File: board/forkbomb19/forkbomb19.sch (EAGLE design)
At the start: 30 parts, among them U1 ESP-WROOM-03

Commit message: drew the tv and started placing stuff
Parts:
- removed U$1: TLC59116-Q1, forkbomb19:TLC59116-Q1
- added C10, C13, C14: 10uF, resistor:C-USC1210
- added C11: 2.2uF, adafruit:C-USC0805
- added C12: 0.1uF, adafruit:C-USC0805
- added C62: 1F, resistor:CPOL-USE5-8.5
- added CHRG/LBO: ORANGE, piboy_new:ADAFRUIT_LEDCHIPLED_0603
- added CN1: LIPO, adafruit:JST_2PIN-SMT-RA
- added D1: MBRS130LT3, diode:MBRS130LT3
- added DONE: GREEN, piboy_new:ADAFRUIT_LEDCHIPLED_0603
- added L1: 6.8uH, microbuilder:INDUCTORTDK_VLC5045
- added LBO: RED, piboy_new:ADAFRUIT_LEDCHIPLED_0603
- added LOGO_B, LOGO_G, LOGO_R: REVERSE_PLCC_LED, forkbomb19:REVERSE_PLCC_LED
- added ON: BLUE, piboy_new:ADAFRUIT_LEDCHIPLED_0603
- added R10: 1.12M, resistor:R-US_R0603
- added R11: 200K, resistor:R-US_R0603
- added R12: 340K, adafruit:R-US_R0805
- added R13: 200K, adafruit:R-US_R0805
- added R14: 1.87M, adafruit:R-US_R0805
- added R15: 270K, resistor:R-US_R0603
- added R16, R21: 100K, resistor:R-US_R0603
- added R17, R18, R20, R9: 1K, resistor:R-US_R0603
- added R19: 1.0K, resistor:R-US_R0603
- added R22: 68, resistor:R-US_R0805
- added T3: MMUN2133LT1G, piboy_new:TRANSISTOR_MUN2113T1-PNP_DRIVER-SC59-BEC
- added THERM: 15K, resistor:R-US_R0603
- added U$17: CL-SB-12A-02T, defcon:CL-SB-12A-02T
- added U4: TPS61090RSAR, microbuilder:VREG_TPS6103X
- added U5: MCP73871, microbuilder:MCP73871
- C1: value (none) -> 100nF; device resistor:C-USC0805 -> resistor:C-USC0603
- C4, C9: device resistor:C-USC0805 -> resistor:C-USC0603
- R1, R6, R7: device resistor:R-US_R0805 -> resistor:R-US_R0603
- R8: value ILED -> 68
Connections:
- removed net RDY_2_SEND: U3G$1.RTS
- new net BOOST_ENABLE: R13.2, U$17.P$2, U4.EN
- new net LBO: T3.B, U4.LBO
- new net N$16: L1.2, U4.SW
- new net N$17: R12.2, R14.1, U4.LBI
- new net N$18: LBO.A, R20.1
- new net N$19: R10.1, R11.2, U4.FB
- new net N$20: R20.2, T3.C
- new net N$21: ON.A, R9.2
- new net N$22: R15.1, R16.1, U5.VPCC
- new net N$23: R18.1, U5.STAT2
- new net N$24: R17.1, U5.STAT1/LBO
- new net N$25: R19.2, U5.PROG1
- new net N$26: THERM.2, U5.THERM
- new net N$27: DONE.C, R18.2
- new net N$28: CHRG/LBO.C, R17.2
- new net N$29: R21.2, U5.PROG3
- new net N$30: CN1.2, D1.A
- new net N$31: LOGO_G.A, R8.2
- new net VBAT: C10.1, C12.1, L1.1, R13.1, R14.2, T3.E, U4.VBAT, U5.VOUT1, U5.VOUT2
- new net VBUS: CHRG/LBO.A, DONE.A, R15.2, U5./TE, U5.CE, U5.PROG2, U5.SEL, U5.VIN1, U5.VIN2
- new net VLIPO: C14.1, D1.C, U5.VBAT1, U5.VBAT2, U5.VBATSENS
- net +3V3: now also C11.1, C13.1, C62.+, LOGO_B.A, R10.2, R22.1, R8.1, R9.1, U4.VOUT; no longer U$1.VCC
- net EN: no longer U$1.RESET
- net GND: now also C10.2, C11.2, C12.2, C13.2, C14.2, C62.-, CN1.1, LBO.C, LOGO_B.C, LOGO_G.C, LOGO_R.C, ON.C, R11.1, R12.1, R16.2, R19.1, R21.1, THERM.1, U$17.P$3, U4.GND, U4.PGND, U4.SYNC, U5.THERMAL, U5.VSS1, U5.VSS2; no longer R8.1, U$1.A0, U$1.A1, U$1.A2, U$1.A3, U$1.GND
- net I2C_SCL: no longer U$1.SCL
- net I2C_SDA: no longer U$1.SDA
- net N$12: now also LOGO_R.A, R22.2; no longer R8.2, U$1.REXT
- net RDY_2_SND: now also U3G$1.RTS
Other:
- note added: "1.0K = 1000mA"
- note added: "10K NTC Thermistor:"
- note added: "2.0K = 500mA"
- note added: "6.8uH power w/2A current"
- note added: "Charge Rate = 1000V/PROG1"
- note added: "No Thermistor:"
- note added: "RT1 = 0, RT2 = 10K"
- note added: "RT1 = TBD, RT2 = TBD"
- note added: "See Pg 15 1st para"
- moved on the sheet: C8, C9, R6, R7, R8, T1, T2, U3G$1, U3G$2, X1

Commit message: more layout work on the board
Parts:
- removed C13, C14: 10uF, resistor:C-USC1210
- removed C62: 1F, resistor:CPOL-USE5-8.5
- removed CHRG/LBO: ORANGE, piboy_new:ADAFRUIT_LEDCHIPLED_0603
- removed CN1: LIPO, adafruit:JST_2PIN-SMT-RA
- removed DONE: GREEN, piboy_new:ADAFRUIT_LEDCHIPLED_0603
- removed LBO: RED, piboy_new:ADAFRUIT_LEDCHIPLED_0603
- removed ON: BLUE, piboy_new:ADAFRUIT_LEDCHIPLED_0603
- removed R12: 340K, adafruit:R-US_R0805
- removed R13: 200K, adafruit:R-US_R0805
- removed R14: 1.87M, adafruit:R-US_R0805
- removed R15: 270K, resistor:R-US_R0603
- removed R16, R21: 100K, resistor:R-US_R0603
- removed R17, R18, R20: 1K, resistor:R-US_R0603
- removed R19: 1.0K, resistor:R-US_R0603
- removed R2: 10K, pot:TRIM_US-B64Y
- removed T3: MMUN2133LT1G, piboy_new:TRANSISTOR_MUN2113T1-PNP_DRIVER-SC59-BEC
- removed THERM: 15K, resistor:R-US_R0603
- removed U4: TPS61090RSAR, microbuilder:VREG_TPS6103X
- removed U5: MCP73871, microbuilder:MCP73871
- added D2: MBRS130LT3, diode:MBRS130LT3
- added U$1: LM2623, forkbomb19:LM2623
- added X2: 22-23-2021, con-molex:22-23-2021
- added X3: POT_GND, con-samtec:TSW-101-07-G-S
- added X4: POT_3V3, con-samtec:TSW-101-07-G-S
- added X5: POT_SIG, con-samtec:TSW-101-07-G-S
- C10: value 10uF -> 22uF; device resistor:C-USC1210 -> resistor:CPOL-US153CLV-0405
- C11: value 2.2uF -> 4.7pF; device adafruit:C-USC0805 -> resistor:C-USC0603
- C12: value 0.1uF -> 10uF; device adafruit:C-USC0805 -> resistor:CPOL-US153CLV-0405
- L1: value 6.8uH -> 4.7uH; device microbuilder:INDUCTORTDK_VLC5045 -> resistor:L-USWE-TPC
- R10: value 1.12M -> 165k
- R11: value 200K -> 100k
- R9: value 1K -> 150k
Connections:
- net SCRN_D0 renamed SCRN_CLK
- net SCRN_D1 renamed SCRN_MOSI
- net SCRN_D3 renamed TSCRN_X2
- net SCRN_D4 renamed TSCRN_X1
- net SCRN_D5 renamed TSCRN_Y2
- net SCRN_D6 renamed TSCRN_Y1
- net SCRN_D7 renamed SCRN_MISO
- removed net BOOST_ENABLE: R13.2, U$17.P$2, U4.EN
- removed net LBO: T3.B, U4.LBO
- removed net N$19: R10.1, R11.2, U4.FB
- removed net N$20: R20.2, T3.C
- removed net N$21: ON.A, R9.2
- removed net N$22: R15.1, R16.1, U5.VPCC
- removed net N$23: R18.1, U5.STAT2
- removed net N$24: R17.1, U5.STAT1/LBO
- removed net N$25: R19.2, U5.PROG1
- removed net N$26: THERM.2, U5.THERM
- removed net N$27: DONE.C, R18.2
- removed net N$28: CHRG/LBO.C, R17.2
- removed net N$29: R21.2, U5.PROG3
- removed net SCRN_D2: U1.IO13
- removed net SCRN_RDX: U1.IO5
- removed net SCRN_WRX: U1.IO17
- removed net VBAT: C10.1, C12.1, L1.1, R13.1, R14.2, T3.E, U4.VBAT, U5.VOUT1, U5.VOUT2
- removed net VBUS: CHRG/LBO.A, DONE.A, R15.2, U5./TE, U5.CE, U5.PROG2, U5.SEL, U5.VIN1, U5.VIN2
- removed net VLIPO: C14.1, D1.C, U5.VBAT1, U5.VBAT2, U5.VBATSENS
- new net N$13: C10.+, D1.C, L1.1, R9.2
- new net N$14: C11.2, R9.1, U$1.FREQ
- new net N$15: C11.1, D2.A, L1.2, U$1.SW
- new net SCRN_RST: U1.IO18
- net +3V3: now also C12.+, D2.C, X4.1; no longer C11.1, C13.1, C62.+, R10.2, R2.A, R9.1, U4.VOUT
- net GND: now also C10.-, C12.-, U$1.PGND, U$1.SGND, U$17.P$1, X2-2.S, X3.1; no longer C10.2, C11.2, C12.2, C13.2, C14.2, C62.-, CN1.1, LBO.C, ON.C, R12.1, R16.2, R19.1, R2.E, R21.1, THERM.1, U$17.P$3, U4.GND, U4.PGND, U4.SYNC, U5.THERMAL, U5.VSS1, U5.VSS2
- net N$16: now also R10.2, U$1.BOOT, U$1.VDD, U$17.P$3; no longer L1.2, U4.SW
- net N$17: now also U$1.EN, U$17.P$2; no longer R12.2, R14.1, U4.LBI
- net N$18: now also R10.1, R11.2, U$1.FB; no longer LBO.A, R20.1
- net N$30: now also X2-1.S; no longer CN1.2
- net N$4: now also X5.1; no longer R2.S
- net SCRN_CSX: now also U1.IO17; no longer U1.IO18
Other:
- note removed: "1.0K = 1000mA"
- note removed: "10K NTC Thermistor:"
- note removed: "2.0K = 500mA"
- note removed: "6.8uH power w/2A current"
- note removed: "Charge Rate = 1000V/PROG1"
- note removed: "No Thermistor:"
- note removed: "RT1 = 0, RT2 = 10K"
- note removed: "RT1 = TBD, RT2 = TBD"
- note removed: "See Pg 15 1st para"
- moved on the sheet: C11, C4, C5, C6, C7, C8, C9, D1, LOGO_B, LOGO_G, LOGO_R, R10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

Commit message: better layout, made room for AA's
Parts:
- removed S1: SFT_RST, SparkFun-Switches:MOMENTARY-SWITCH-SPST-SMD-6.0X3.5MM
- added SW1: SPST_TACT-KMR2, adafruit:SPST_TACT-KMR2
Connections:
- net GND: now also SW1.S, SW1.S1; no longer S1.2
- net N$2: now also SW1.P, SW1.P1; no longer S1.1
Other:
- moved on the sheet: C4, C5, C6, C7, C8, C9, LOGO_B, LOGO_G, LOGO_R, R22, R3, R4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

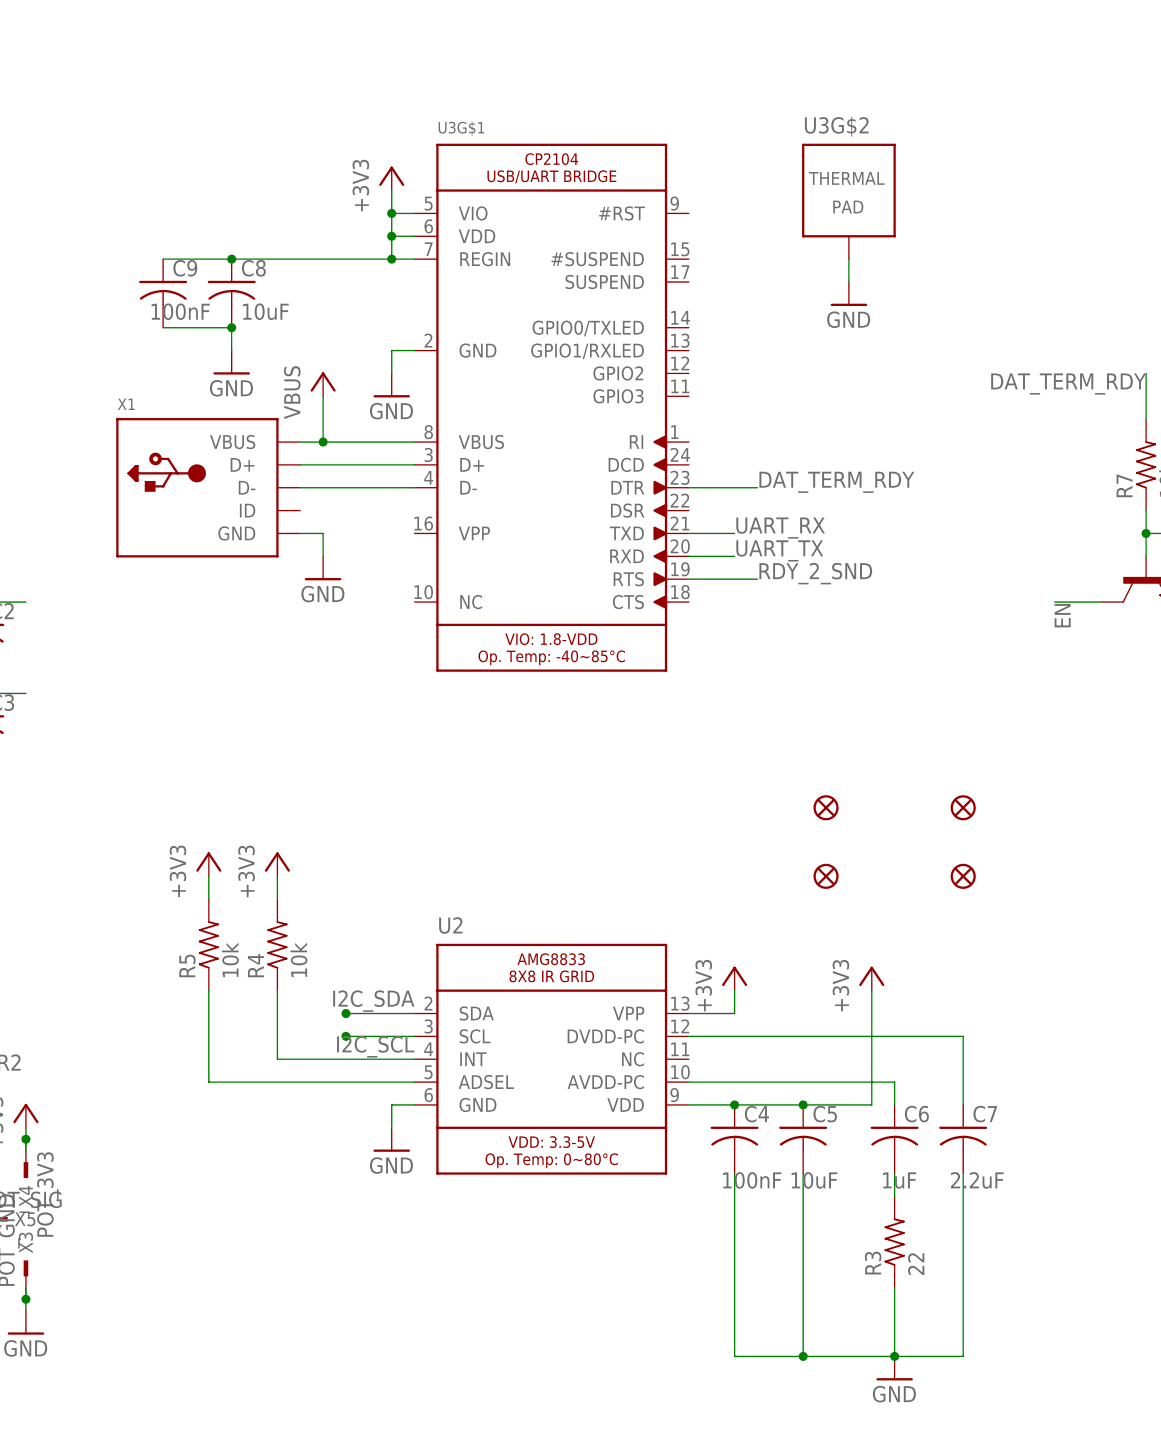
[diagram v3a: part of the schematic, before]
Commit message: more layout work, trying to remove excess vias
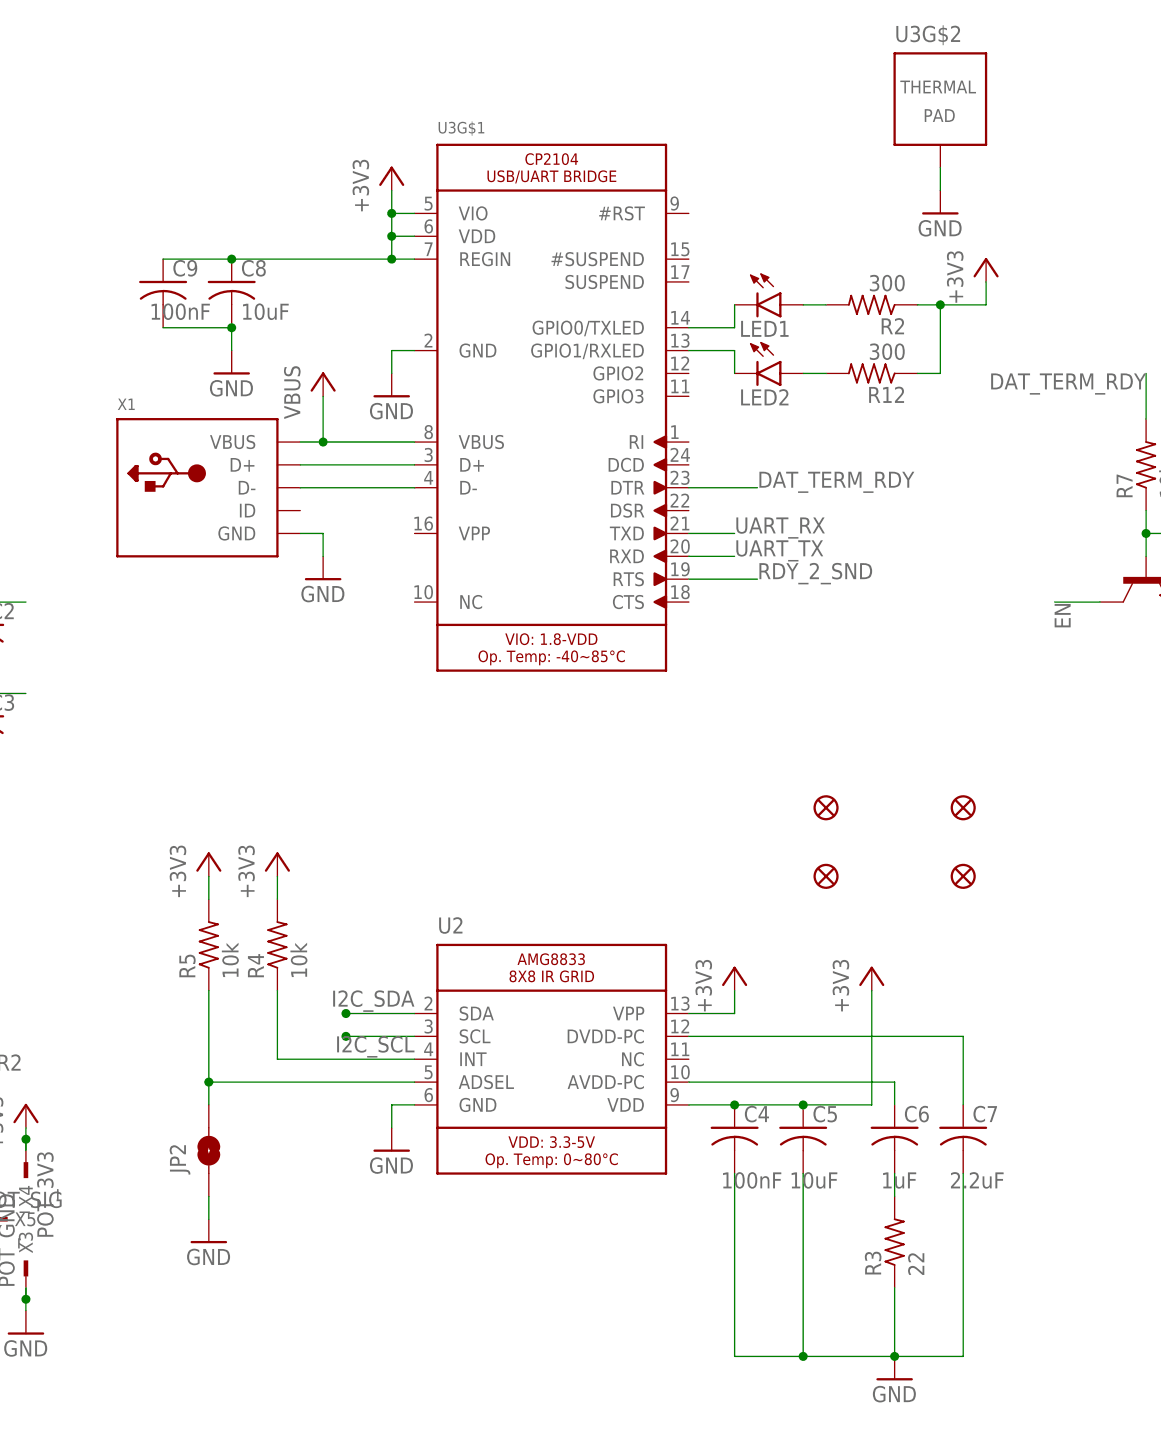
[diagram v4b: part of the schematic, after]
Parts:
- added JP2: JUMPER-SMT_2_NO_SILK_ROUND, SparkFun-Jumpers:JUMPER-SMT_2_NO_SILK_ROUND
- added LED1, LED2: (no value), led:LEDSML0603
- added R12, R2: 300, resistor:R-US_R0603
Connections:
- new net N$19: LED2.C, U3G$1.GPIO1/RXLED
- new net N$20: LED1.C, U3G$1.GPIO0/TXLED
- new net N$21: LED1.A, R2.2
- new net N$22: LED2.A, R12.2
- net +3V3: now also R12.1, R2.1
- net GND: now also JP2.1
- net N$7: now also JP2.2
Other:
- moved on the sheet: U3G$2
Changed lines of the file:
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@@
 <part name="X5" library="con-samtec" library_urn="urn:adsk.eagle:library:184" deviceset="TSW-101-*-G-S" device="" technology="07" value="POT_SIG"/>
 <part name="SW1" library="adafruit" library_urn="urn:adsk.eagle:library:420" deviceset="SPST_TACT" device="-KMR2" package3d_urn="urn:adsk.eagle:package:6240885/1"/>
+<part name="LED1" library="led" library_urn="urn:adsk.eagle:library:259" deviceset="LED" device="SML0603" package3d_urn="urn:adsk.eagle:package:15832/1"/>
+<part name="LED2" library="led" library_urn="urn:adsk.eagle:library:259" deviceset="LED" device="SML0603" package3d_urn="urn:adsk.eagle:package:15832/1"/>
+<part name="R2" library="resistor" library_urn="urn:adsk.eagle:library:348" deviceset="R-US_" device="R0603" package3d_urn="urn:adsk.eagle:package:23555/2" value="300"/>
+<part name="R12" library="resistor" library_urn="urn:adsk.eagle:library:348" deviceset="R-US_" device="R0603" package3d_urn="urn:adsk.eagle:package:23555/2" value="300"/>
+<part name="+3V12" library="supply1" library_urn="urn:adsk.eagle:library:371" deviceset="+3V3" device=""/>
+<part name="JP2" library="SparkFun-Jumpers" library_urn="urn:adsk.eagle:library:528" deviceset="JUMPER-SMT_2_NO" device="_SILK_ROUND" package3d_urn="urn:adsk.eagle:package:39280/1" value=""/>
+<part name="GND18" library="supply1" library_urn="urn:adsk.eagle:library:371" deviceset="GND" device=""/>
 </parts>
 <sheets>
@@
 <attribute name="VALUE" x="111.76" y="20.32" size="1.27" layer="96"/>
 </instance>
-<instance part="U3" gate="G$2" x="157.48" y="76.2" smashed="yes">
-<attribute name="NAME" x="152.4" y="82.55" size="1.778" layer="95"/>
+<instance part="U3" gate="G$2" x="167.64" y="86.36" smashed="yes">
+<attribute name="NAME" x="162.56" y="92.71" size="1.778" layer="95"/>
 </instance>
 <instance part="FID1" gate="G$1" x="154.94" y="7.62" smashed="yes"/>
@@
 <attribute name="VALUE" x="76.2" y="33.02" size="1.27" layer="96"/>
 </instance>
-<instance part="GND8" gate="1" x="157.48" y="63.5" smashed="yes">
-<attribute name="VALUE" x="154.94" y="60.96" size="1.778" layer="96"/>
+<instance part="GND8" gate="1" x="167.64" y="73.66" smashed="yes">
+<attribute name="VALUE" x="165.1" y="71.12" size="1.778" layer="96"/>
 </instance>
 <instance part="GND9" gate="1" x="99.06" y="33.02" smashed="yes">
@@
 <attribute name="NAME" x="40.64" y="-19.05" size="1.778" layer="95"/>
 <attribute name="VALUE" x="46.355" y="-21.59" size="1.778" layer="96"/>
+</instance>
+<instance part="LED1" gate="G$1" x="149.86" y="63.5" smashed="yes" rot="R270">
+<attribute name="NAME" x="145.288" y="59.944" size="1.778" layer="95"/>
+<attribute name="VALUE" x="145.288" y="57.785" size="1.778" layer="96"/>
+</instance>
+<instance part="LED2" gate="G$1" x="149.86" y="55.88" smashed="yes" rot="R270">
+<attribute name="NAME" x="145.288" y="52.324" size="1.778" layer="95"/>
+<attribute name="VALUE" x="145.288" y="50.165" size="1.778" layer="96"/>
+</instance>
+<instance part="R2" gate="G$1" x="160.02" y="63.5" smashed="yes" rot="R180">
+<attribute name="NAME" x="163.83" y="62.0014" size="1.778" layer="95" rot="R180"/>
+<attribute name="VALUE" x="163.83" y="66.802" size="1.778" layer="96" rot="R180"/>
+</instance>
+<instance part="R12" gate="G$1" x="160.02" y="55.88" smashed="yes" rot="R180">
+<attribute name="NAME" x="163.83" y="54.3814" size="1.778" layer="95" rot="R180"/>
+<attribute name="VALUE" x="163.83" y="59.182" size="1.778" layer="96" rot="R180"/>
+</instance>
+<instance part="+3V12" gate="G$1" x="172.72" y="68.58" smashed="yes">
+<attribute name="VALUE" x="170.18" y="63.5" size="1.778" layer="96" rot="R90"/>
+</instance>
+<instance part="JP2" gate="G$1" x="86.36" y="-30.48" smashed="yes" rot="R90">
+<attribute name="NAME" x="83.82" y="-33.02" size="1.778" layer="95" font="vector" rot="R90"/>
+<attribute name="VALUE" x="88.9" y="-33.02" size="1.778" layer="96" font="vector" rot="R90" align="top-left"/>
+</instance>
+<instance part="GND18" gate="1" x="86.36" y="-40.64" smashed="yes">
+<attribute name="VALUE" x="83.82" y="-43.18" size="1.778" layer="96"/>
 </instance>
 </instances>
@@
 <junction x="-114.3" y="30.48"/>
 </segment>
+<segment>
+<pinref part="R12" gate="G$1" pin="1"/>
+<wire x1="165.1" y1="55.88" x2="167.64" y2="55.88" width="0.1524" layer="91"/>
+<wire x1="167.64" y1="55.88" x2="167.64" y2="63.5" width="0.1524" layer="91"/>
+<pinref part="R2" gate="G$1" pin="1"/>
+<wire x1="167.64" y1="63.5" x2="165.1" y2="63.5" width="0.1524" layer="91"/>
+<wire x1="167.64" y1="63.5" x2="172.72" y2="63.5" width="0.1524" layer="91"/>
+<junction x="167.64" y="63.5"/>
+<pinref part="+3V12" gate="G$1" pin="+3V3"/>
+<wire x1="172.72" y1="63.5" x2="172.72" y2="66.04" width="0.1524" layer="91"/>
+</segment>
 </net>
 <net name="EN" class="0">
@@
 <pinref part="GND8" gate="1" pin="GND"/>
 <pinref part="U3" gate="G$2" pin="TP"/>
-<wire x1="157.48" y1="66.04" x2="157.48" y2="68.58" width="0.1524" layer="91"/>
+<wire x1="167.64" y1="76.2" x2="167.64" y2="78.74" width="0.1524" layer="91"/>
 </segment>
 <segment>
@@
 <wire x1="-114.3" y1="17.78" x2="-114.3" y2="20.32" width="0.1524" layer="91"/>
 </segment>
+<segment>
+<pinref part="JP2" gate="G$1" pin="1"/>
+<pinref part="GND18" gate="1" pin="GND"/>
+<wire x1="86.36" y1="-35.56" x2="86.36" y2="-38.1" width="0.1524" layer="91"/>
+</segment>
 </net>
 <net name="N$2" class="0">
@@
 <pinref part="R5" gate="G$1" pin="1"/>
 <wire x1="86.36" y1="-22.86" x2="86.36" y2="-12.7" width="0.1524" layer="91"/>
+<wire x1="86.36" y1="-22.86" x2="86.36" y2="-25.4" width="0.1524" layer="91"/>
+<junction x="86.36" y="-22.86"/>
+<pinref part="JP2" gate="G$1" pin="2"/>
 </segment>
 </net>
@@
 </segment>
 </net>
+<net name="N$19" class="0">
+<segment>
+<pinref part="U3" gate="G$1" pin="GPIO1/RXLED"/>
+<wire x1="139.7" y1="58.42" x2="144.78" y2="58.42" width="0.1524" layer="91"/>
+<pinref part="LED2" gate="G$1" pin="C"/>
+<wire x1="144.78" y1="58.42" x2="144.78" y2="55.88" width="0.1524" layer="91"/>
+</segment>
+</net>
+<net name="N$20" class="0">
+<segment>
+<pinref part="U3" gate="G$1" pin="GPIO0/TXLED"/>
+<wire x1="139.7" y1="60.96" x2="144.78" y2="60.96" width="0.1524" layer="91"/>
+<pinref part="LED1" gate="G$1" pin="C"/>
+<wire x1="144.78" y1="60.96" x2="144.78" y2="63.5" width="0.1524" layer="91"/>
+</segment>
+</net>
+<net name="N$21" class="0">
+<segment>
+<pinref part="R2" gate="G$1" pin="2"/>
+<pinref part="LED1" gate="G$1" pin="A"/>
+<wire x1="154.94" y1="63.5" x2="152.4" y2="63.5" width="0.1524" layer="91"/>
+</segment>
+</net>
+<net name="N$22" class="0">
+<segment>
+<pinref part="R12" gate="G$1" pin="2"/>
+<pinref part="LED2" gate="G$1" pin="A"/>
+<wire x1="154.94" y1="55.88" x2="152.4" y2="55.88" width="0.1524" layer="91"/>
+</segment>
+</net>
